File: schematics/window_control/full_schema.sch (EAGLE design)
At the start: 68 parts, among them IC1 MEGA32-P, J1 SERVO, J2 J2, J3 J2, J4 J2, J5 J2, Q16 2N3906BU, Q17 STP14NM50N, Q2 2N3904, Q4 2N3904, Q5 2N3904, SW1 SWITCH, U1 ESP32, U10 LM311P, U3 BMP280 / 5V, U4 MSGEQ7, U6 GY-SGP30, U7 433MHZ_TRANSMITTER, U8 NE555P, U9 SN74LS32N, X1 HC-49S (16MHZ)

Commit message: actualized some nominals in schematics
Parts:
- removed C16: 10 uF, my_devices:C
- removed C17: 5nF, my_devices:C-1
- removed C18: 1000 uF, my_devices:C
- removed C19: 10 pF, my_devices:C-1
- removed C20: 80 pF, my_devices:C-1
- removed Q17: STP14NM50N, my_devices:MOSFET_N
- removed U9: SN74LS32N, my_devices:SN74LS32N
- added C11: 0.22 uF, my_devices:C
- added C12: 4.7 nF, my_devices:C-1
- added C13: 0.1 uF, my_devices:C-1
- added C14: 33 pF, my_devices:C-1
- added C8: 22 pF, my_devices:C-1
- added Q6: 2N3904, my_devices:TRANSISTOR_NPN
- added U5: BMP280 / 5V, my_devices:BME280
- C1: value 0.22 uF -> 5nF; device my_devices:C -> my_devices:C-1
- C10: value 33 pF -> 10 uF; device my_devices:C-1 -> my_devices:C
- C2: value 22 pF -> 1000 uF; device my_devices:C-1 -> my_devices:C
- C3: value 22 pF -> 10 pF
- C4: value 4.7 nF -> 80 pF
- C6: value 0.22 uF -> 1000 uF
- C7: value 1000 uF -> 22 pF; device my_devices:C -> my_devices:C-1
- C9: value 0.1 uF -> 0.22 uF; device my_devices:C-1 -> my_devices:C
- D1: value LD -> GNL-3014ED
- D2, D3: value 1N4001 -> BAT41
- J1: value SERVO -> MTR-SERVO-FS5103B
- Q1: value (none) -> 2N3904
- Q5: value 2N3904 -> STP14NM50N; device my_devices:TRANSISTOR_NPN -> my_devices:MOSFET_N
- R1, R4: value R -> 620
- R10: value 620 -> 100
- R12: value 620 -> 10K
- R13: value 200K -> 100
- R14: value 10K -> 5
- R15: value 200K -> 3K
- R16: value 200 -> 10K
- R17: value 5 -> 200K
- R18: value 200k -> 200K
- R19: value 620 -> 5K; device my_devices:R -> my_devices:RD
- R2: value R -> 100
- R20: value 150K -> 10K
- R21: value 5K -> 200k; device my_devices:RD -> my_devices:R
- R3: value 10K -> 150K
- R5: value 100 -> 620
- R6: value 3K -> 620
- R7: value 20K -> 620; device my_devices:RD -> my_devices:R
- R8: value 100 -> 20K; device my_devices:R -> my_devices:RD
- R9: value 620 -> 200
- U3: value BMP280 / 5V -> NE555P; device my_devices:BME280 -> my_devices:NE555P
- U4: value MSGEQ7 -> SN74LS32N; device my_devices:MSGEQ7 -> my_devices:SN74LS32N
- U6: value GY-SGP30 -> 433MHZ_TRANSMITTER; device my_devices:GY-SGP30 -> my_devices:433MHZ_TRANSMITTER
- U7: value 433MHZ_TRANSMITTER -> MSGEQ7; device my_devices:433MHZ_TRANSMITTER -> my_devices:MSGEQ7
- U8: value NE555P -> GY-SGP30; device my_devices:NE555P -> my_devices:GY-SGP30
- renumbered D7 to D3, D8 to D4, D9 to D2, L4 to L1, Q16 to Q3, U10 to U2
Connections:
- net +5V: now also Q5.D, R2.P$2, R3.P$2, U4.VCC; no longer Q17.D, R1.P$2, R20.P$2, U9.VCC
- net +5V_IF_EN: now also C2.PIN_PLUS, R10.P$2, U3.RESET, U3.VCC; no longer C18.PIN_PLUS, R8.P$2, U8.RESET, U8.VCC
- net 3V3: now also R11.P$1, R12.P$2; no longer R11.P$2, R4.P$1
- net GND: now also C2.PIN_GND, C3.P$2, C4.P$1, C5.PIN_GND, R15.P$1, R9.P$2, U3.GND, U4.1B, U4.GND; no longer C16.PIN_GND, C18.PIN_GND, C19.P$2, C20.P$1, R16.P$2, R6.P$1, U8.GND, U9.1B, U9.GND
- net HALL_OUT_INV: now also R12.P$1, R7.P$2, U4.1A; no longer R11.P$1, R12.P$2, U9.1A
- net I2C_SCL: now also U5.SCL, U8.SCL; no longer U3.SCL, U6.SCL
- net I2C_SDA: now also U5.SDA, U8.SDA; no longer U3.SDA, U6.SDA
- net LED_CONTROL: now also R1.P$1; no longer R2.P$1
- net N$1: now also R14.P$1; no longer R17.P$1
- net N$11: now also C9.PIN_PLUS, R16.P$2; no longer C1.PIN_PLUS, R3.P$2
- net N$12: now also C9.PIN_GND, Q6.B, R17.P$1, R18.P$2; no longer C1.PIN_GND, Q2.B, R13.P$1, R15.P$2
- net N$13: now also C12.P$1, Q6.C, R19.P2, R19.P3; no longer C4.P$1, Q2.C, R21.P2, R21.P3
- net N$16: now also C10.PIN_PLUS, R20.P$1; no longer C5.PIN_PLUS, R14.P$1
- net N$17: now also C14.P$1, R21.P$1, U7.CKIN; no longer C10.P$1, R18.P$1, U4.CKIN
- net N$18: now also C13.P$1, U7.IGND; no longer C9.P$1, U4.IGND
- net N$19: now also C12.P$2, U7.IN; no longer C4.P$2, U4.IN
- net N$2: now also R13.P$2; no longer R5.P$2
- net N$24: now also C7.P$2; no longer C2.P$2
- net N$26: now also C8.P$2; no longer C3.P$2
- net N$28: now also R6.P$1; no longer R10.P$1
- net N$29: now also R7.P$1; no longer R12.P$1
- net N$3: now also U4.2Y, U4.4B; no longer U9.2Y, U9.4B
- net N$32: now also R4.P$1; no longer R19.P$1
- net N$35: now also R13.P$1, U3.OUT; no longer R5.P$1, U8.OUT
- net N$37: now also Q2.C; no longer Q5.C
- net N$38: now also Q2.E, R9.P$1; no longer Q5.E, R16.P$1
- net N$39: now also R14.P$2; no longer R17.P$2
- net N$40: now also Q5.S; no longer Q17.S
- net N$44: now also C3.P$1, U3.CONT; no longer C19.P$1, U8.CONT
- net N$46: now also C4.P$2, U3.THRES, U3.TRIG; no longer C20.P$2, U8.THRES, U8.TRIG
- net N$47: now also R8.P3, U3.DISCH; no longer R7.P3, U8.DISCH
- net N$48: now also R8.P2; no longer R7.P2
- net N$49: now also R10.P$1, R8.P1; no longer R7.P1, R8.P$1
- net N$5: now also R1.P$2; no longer R2.P$2
- net N$50: now also Q2.B; no longer Q5.B
- net N$51: now also C5.PIN_PLUS, Q5.G, R15.P$2; no longer C16.PIN_PLUS, Q17.G, R6.P$2
- net N$52: now also U4.3A, U4.4Y; no longer U9.3A, U9.4Y
- net N$53: now also C1.P$2, R3.P$1; no longer C17.P$2, R20.P$1
- net N$56: now also U4.1Y, U4.2A; no longer U9.1Y, U9.2A
- net N$6: now also R5.P$1; no longer R9.P$1
- net N$8: now also R2.P$1; no longer R1.P$1
- net NOISE_LEVEL: now also U7.OUT; no longer U4.OUT
- net NOISE_RESET: now also U7.RESET; no longer U4.RESET
- net NOISE_STROBE: now also U7.STROBE; no longer U4.STROBE
- net OUTDOOR_+5V: now also C11.PIN_PLUS, R16.P$1, R17.P$2, R19.P1, R20.P$2, R21.P$2, U5.VCC, U6.VCC, U8.VIN; no longer C7.PIN_PLUS, R13.P$2, R14.P$2, R18.P$2, R21.P1, R3.P$1, U3.VCC, U4.VCC, U6.VIN
- net OUTDOOR_GND: now also C10.PIN_GND, C11.PIN_GND, C13.P$2, C14.P$2, C7.P$1, C8.P$1, Q6.E, R18.P$1, U5.GND, U6.DATA, U7.GND, U8.GND; no longer C10.P$2, C2.P$1, C3.P$1, C5.PIN_GND, C7.PIN_GND, C9.P$2, Q2.E, R15.P$1, U3.GND, U4.GND, U6.GND, U7.DATA
- net SERVO_ENABLE_INV: now also R6.P$2, U4.4A; no longer R10.P$2, U9.4A
- net SERVO_PWM: now also R5.P$2, U4.3B; no longer R9.P$2, U9.3B
- net SERVO_PWM_CONTROL: now also C1.P$1, U4.3Y; no longer C17.P$1, U9.3Y
- net SW_IS_ON_INV: now also R11.P$2, U4.2B; no longer R19.P$2, U9.2B
- net TRANSMITTER: now also U6.GND; no longer U7.GND
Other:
- note added: "~10-15-20V In my case ~12..14V Mosfet required >8V"
- note removed: "~10-15-20V In my case ~12V Mosfet needs >8V"
- moved on the sheet: C3, C4, C5, C6, Q2, R1, R10, R11, R12, R13, R14, R15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

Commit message: Changed Noise sensor schematics. Removed MSGEQ7 chip (replaced with program FFT). I cant find any live. Changed Volume Amplifier from transistors to chio.
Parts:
- removed BM1: EM6050P, my_devices:MICROPHONE
- removed C12: 4.7 nF, my_devices:C-1
- removed C13: 0.1 uF, my_devices:C-1
- removed C14: 33 pF, my_devices:C-1
- removed Q6: 2N3904, my_devices:TRANSISTOR_NPN
- removed R17, R18: 200K, my_devices:R
- removed R19: 5K, my_devices:RD
- removed R21: 200k, my_devices:R
- added BM2: EM6050P, my_devices:MICROPHONE
- added C15: 0.1 uF, my_devices:C-1
- added L2: L, my_devices:L
- added R22: 3K, my_devices:R
- added R23, R26: 200K, my_devices:RD
- added U9: LM358, my_devices:LM358
- C9: value 0.22 uF -> C
- R16: value 10K -> 200K
- U7: value MSGEQ7 -> VOLTAGE_REGULATOR; device my_devices:MSGEQ7 -> my_devices:VOLTAGE_REGULATOR
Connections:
- removed net N$11: BM1.P$2, C9.PIN_PLUS, R16.P$2
- removed net N$12: C9.PIN_GND, Q6.B, R17.P$1, R18.P$2
- removed net N$13: C12.P$1, Q6.C, R19.P2, R19.P3
- removed net N$17: C14.P$1, R21.P$1, U7.CKIN
- removed net N$18: C13.P$1, U7.IGND
- removed net N$19: C12.P$2, U7.IN
- removed net NOISE_RESET: IC1.(ADC7)PA7, U7.RESET
- removed net NOISE_STROBE: IC1.(ADC6)PA6, U7.STROBE
- new net N$14: BM2.P$2, C15.P$1, R22.P$2
- new net N$15: C15.P$2, R16.P$2, U9.A+
- new net N$20: R23.P1, U9.A_OUT, U9.B+
- new net N$21: R23.P3, U9.A-
- new net N$25: R26.P3, U9.B-
- new net OUT: L2.P$1, U7.OUT
- new net OUTDOOR_+2.5V: C9.PIN_PLUS, L2.P$2, R16.P$1, R23.P2, R26.P1
- net NOISE_LEVEL: now also R26.P2, U9.B_OUT; no longer U7.OUT
- net OUTDOOR_+5V: now also R22.P$1, U7.IN, U9.VCC; no longer R16.P$1, R17.P$2, R19.P1, R21.P$2, U7.VCC
- net OUTDOOR_GND: now also BM2.P$1, C9.PIN_GND, U9.VEE; no longer BM1.P$1, C13.P$2, C14.P$2, Q6.E, R18.P$1
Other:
- note removed: "https://cxem.net/sound/light/light82.php"
- moved on the sheet: C9, R16

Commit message: changed schematics. Removed 433MHZ transmitter. Outdoor module will transfer data using ESP32
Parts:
- removed U6: 433MHZ_TRANSMITTER, my_devices:433MHZ_TRANSMITTER
- added J6, J7, J8, J9: J2, my_devices:J2
- added R17: 620, my_devices:R
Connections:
- removed net TRANSMITTER: IC1.(INT1)PD3, U6.GND
- new net N$11: J7.PIN_2, J8.PIN_1
- new net N$12: J7.PIN_1, J8.PIN_2
- new net N$13: R17.P$1, U1.IO2
- new net OUTDOOR_DATA_OUT: IC1.(INT1)PD3, J6.PIN_1
- new net OUTDOOR_SIGNAL: J9.PIN_2, R17.P$2
- net GND: now also J9.PIN_1
- net OUTDOOR_+5V: no longer U6.VCC
- net OUTDOOR_GND: now also J6.PIN_2; no longer U6.DATA
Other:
- note removed: "https://habr.com/ru/post/491530/"
- moved on the sheet: C6, J2, J3, J4, J5, U5, U8

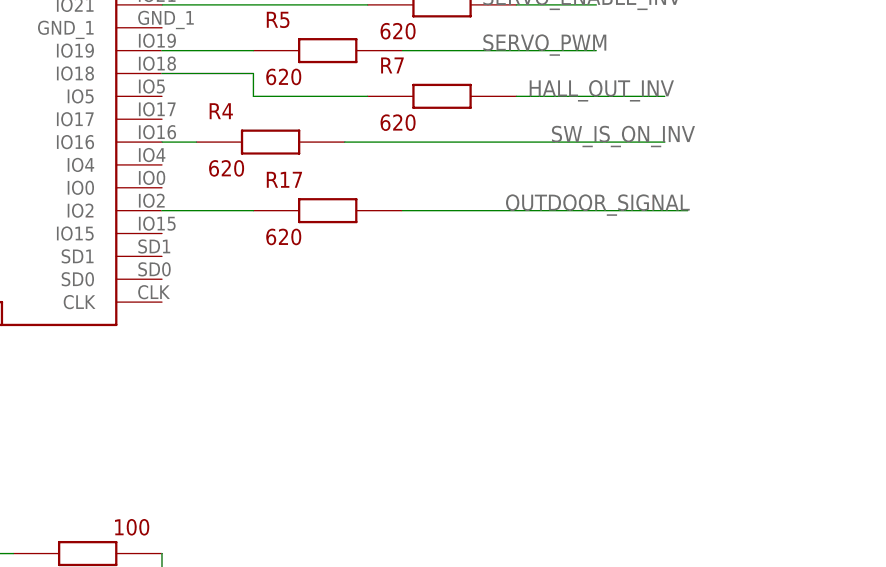
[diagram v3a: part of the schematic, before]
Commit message: Estabilished connection between AVR and ESP32. ESP32 ready to read data from AVR and send it into MQTT
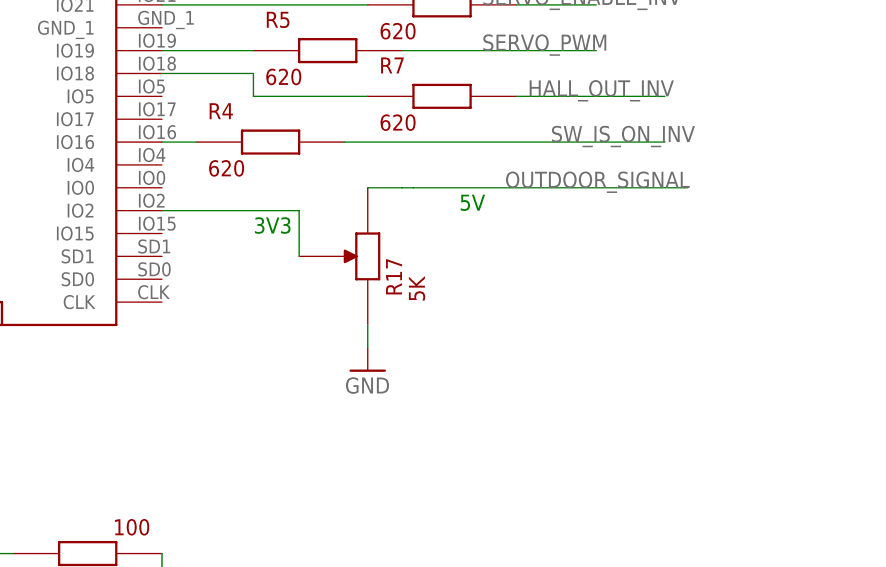
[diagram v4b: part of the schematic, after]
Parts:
- R17: value 620 -> 5K; device my_devices:R -> my_devices:RD
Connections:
- net GND: now also R17.P1
- net N$13: now also R17.P3; no longer R17.P$1
- net OUTDOOR_SIGNAL: now also R17.P2; no longer R17.P$2
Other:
- note added: "3V3"
- note added: "5V"
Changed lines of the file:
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@@
 <part name="J9" library="my_devices" deviceset="J2" device=""/>
 <part name="GND6" library="supply1" library_urn="urn:adsk.eagle:library:371" deviceset="GND" device=""/>
-<part name="R17" library="my_devices" deviceset="R" device="" value="620"/>
+<part name="R17" library="my_devices" deviceset="RD" device="" value="5K"/>
+<part name="GND8" library="supply1" library_urn="urn:adsk.eagle:library:371" deviceset="GND" device=""/>
 </parts>
 <sheets>
@@
 <text x="-111.76" y="337.82" size="5.08" layer="91">Indoor modules</text>
 <text x="256.54" y="342.9" size="5.08" layer="91">Outdoor module</text>
+<text x="-162.56" y="114.3" size="1.778" layer="91" grouprefs="ESP">5V</text>
+<text x="-185.42" y="111.76" size="1.778" layer="91" grouprefs="ESP">3V3</text>
 </plain>
 <instances>
@@
 <attribute name="VALUE" x="58.42" y="109.22" size="1.778" layer="96"/>
 </instance>
-<instance part="R17" gate="G$1" x="-177.8" y="114.3" smashed="yes" grouprefs="ESP">
-<attribute name="NAME" x="-184.15" y="116.84" size="1.778" layer="94"/>
-<attribute name="VALUE" x="-184.15" y="110.49" size="1.778" layer="94"/>
+<instance part="R17" gate="G$1" x="-172.72" y="109.22" smashed="yes" rot="R90" grouprefs="ESP">
+<attribute name="NAME" x="-168.91" y="104.775" size="1.778" layer="94" rot="R90"/>
+<attribute name="VALUE" x="-166.37" y="104.14" size="1.778" layer="94" rot="R90"/>
+</instance>
+<instance part="GND8" gate="1" x="-172.72" y="96.52" smashed="yes" grouprefs="ESP">
+<attribute name="VALUE" x="-175.26" y="93.98" size="1.778" layer="96"/>
 </instance>
 </instances>
@@
 <pinref part="J9" gate="G$1" pin="PIN_1"/>
 <wire x1="60.96" y1="114.3" x2="66.04" y2="114.3" width="0.1524" layer="91" grouprefs="INDOOR_TO_OUTDOOR_CABEL"/>
+</segment>
+<segment>
+<pinref part="R17" gate="G$1" pin="P1"/>
+<pinref part="GND8" gate="1" pin="GND"/>
+<wire x1="-172.72" y1="101.6" x2="-172.72" y2="99.06" width="0.1524" layer="91" grouprefs="ESP"/>
 </segment>
 </net>
@@
 </segment>
 <segment>
-<pinref part="R17" gate="G$1" pin="P$2"/>
-<wire x1="-168.91" y1="114.3" x2="-137.16" y2="114.3" width="0.1524" layer="91" grouprefs="ESP"/>
-<label x="-157.48" y="114.3" size="1.778" layer="95" grouprefs="ESP"/>
+<wire x1="-168.91" y1="116.84" x2="-167.64" y2="116.84" width="0.1524" layer="91" grouprefs="ESP"/>
+<label x="-157.48" y="116.84" size="1.778" layer="95" grouprefs="ESP"/>
+<pinref part="R17" gate="G$1" pin="P2"/>
+<wire x1="-167.64" y1="116.84" x2="-137.16" y2="116.84" width="0.1524" layer="91" grouprefs="ESP"/>
+<wire x1="-168.91" y1="116.84" x2="-172.72" y2="116.84" width="0.1524" layer="91" grouprefs="ESP"/>
 </segment>
 </net>
@@
 <segment>
 <pinref part="U1" gate="G$1" pin="IO2"/>
-<pinref part="R17" gate="G$1" pin="P$1"/>
-<wire x1="-195.58" y1="114.3" x2="-185.42" y2="114.3" width="0.1524" layer="91" grouprefs="ESP"/>
-</segment>
-</net>
+<wire x1="-195.58" y1="114.3" x2="-180.34" y2="114.3" width="0.1524" layer="91" grouprefs="ESP"/>
+<pinref part="R17" gate="G$1" pin="P3"/>
+<wire x1="-180.34" y1="114.3" x2="-180.34" y2="109.22" width="0.1524" layer="91" grouprefs="ESP"/>
+</segment>
+</net>
